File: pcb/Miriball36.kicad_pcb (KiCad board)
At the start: 2 copper layers, 124.8 x 99.1 mm, 45 parts, among them J2 MJ-4PP-9, SW1 SW_PUSH, SW10 SW_PUSH, SW11 SW_PUSH, SW12 SW_PUSH, SW13 SW_PUSH, SW14 SW_PUSH, SW15 SW_PUSH, SW16 SW_PUSH, SW17 SW_PUSH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

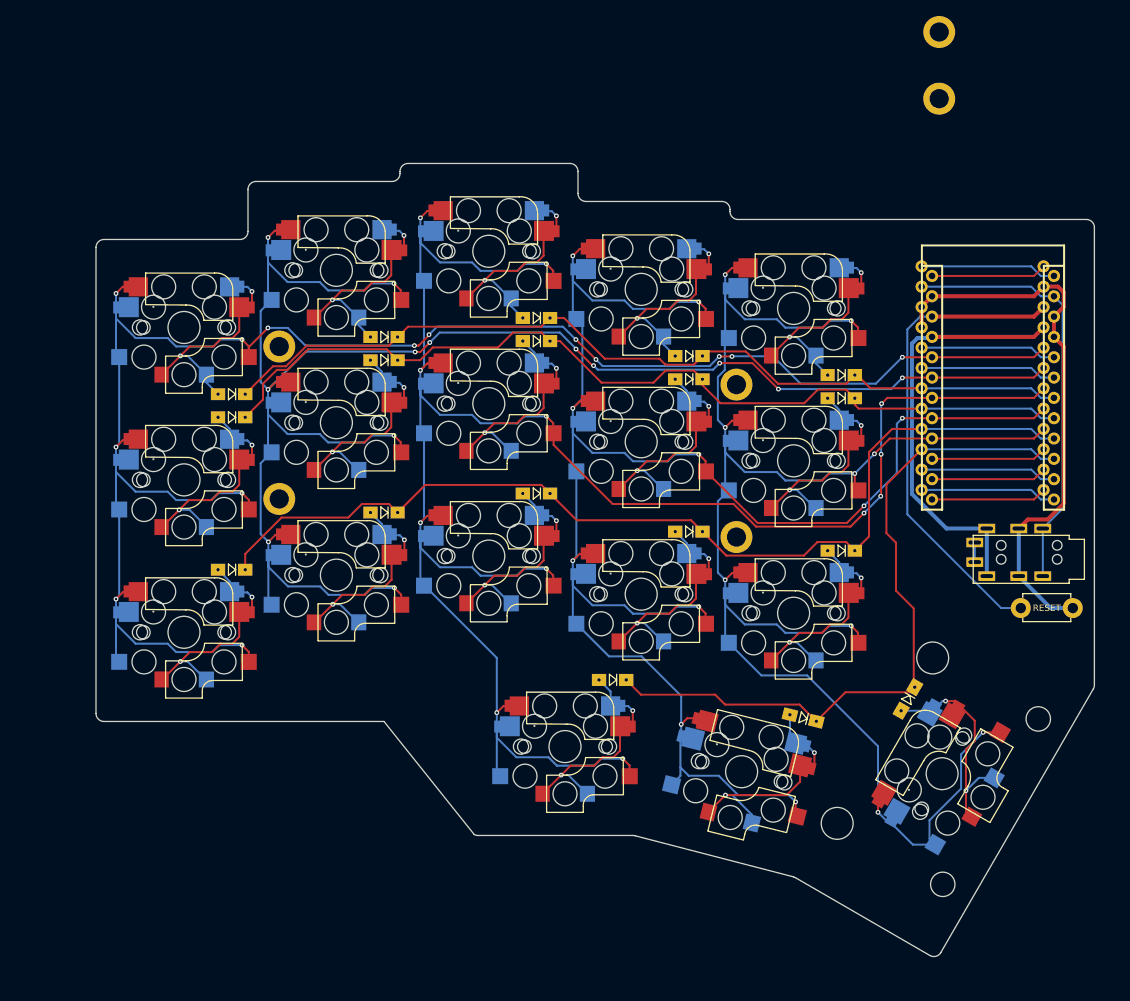
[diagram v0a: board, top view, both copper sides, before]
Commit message: add logo & pin for trackball
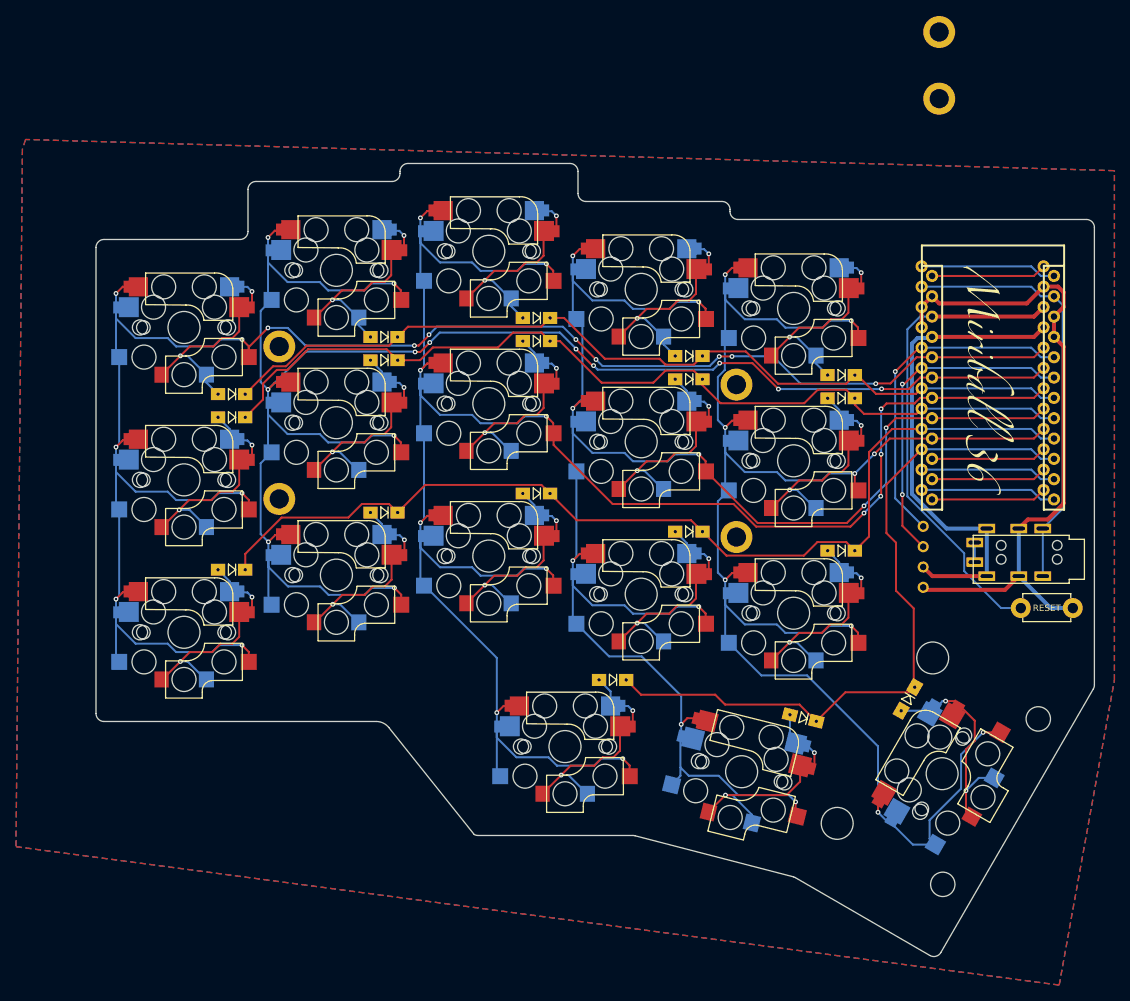
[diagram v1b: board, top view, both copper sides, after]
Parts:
- added G***: LOGO, daiki_daiku_footprints:logo, F.Cu at (157.9, 65.2)
- added OL1: OLED, yuuichi_kbd:OLED_4Pin, F.Cu at (150.2, 87.2)
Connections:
- U1 pad 5: unconnected-(U1-2/D1/SDA-Pad5) -> sda
- U1 pad 6: unconnected-(U1-3/D0/SCL-Pad6) -> scl
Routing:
- net sda: track 0.00 -> 42.4 mm, vias 0 -> 1
- net scl: track 0.00 -> 41.9 mm, vias 0 -> 2
- net unconnected-(U1-3/D0/SCL-Pad6): track 17.0 -> 0.00 mm
- net unconnected-(U1-2/D1/SDA-Pad5): track 17.0 -> 0.00 mm
- net GND: track 70.3 -> 83.9 mm
- net VCC: track 53.2 -> 61.6 mm
- net row0: track 111.4 -> 112.0 mm
- net row1: track 115.8 -> 116.3 mm
- added copper zone on B.Cu, net GND
- added copper zone on F.Cu, net GND
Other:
- outline, holes or cut-outs redrawn

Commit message: add hole
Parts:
- moved H6 71.4 mm to (145.7, 101.0)
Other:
- board text added: "Miriball36 v1.0 PCB Designed by Mimoto & daiki_daiku"
- board text removed: "Miriball39 v1.0 PCB Designed by Mimoto & Mori"
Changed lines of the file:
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@@
 		(fp_arc
 			(start 0.225 -2.8)
-			(mid 1.74436 -2.328061)
+			(mid 1.744359 -2.328061)
 			(end 2.485 -0.920001)
 			(stroke
@@
 		(fp_arc
 			(start 2.57 1.400001)
-			(mid 1.834421 2.975843)
+			(mid 1.834422 2.975844)
 			(end 0.2 3.57)
 			(stroke
@@
 		(fp_arc
 			(start -3.5 6.03)
-			(mid -2.595909 6.48733)
+			(mid -2.59591 6.487331)
 			(end -2.28 7.45)
 			(stroke
@@
 		(fp_arc
 			(start -2.485 -0.920001)
-			(mid -1.74436 -2.328062)
+			(mid -1.74436 -2.328061)
 			(end -0.225 -2.8)
 			(stroke
@@
 		(fp_arc
 			(start 2.57 1.4)
-			(mid 1.834422 2.975842)
+			(mid 1.83442 2.975841)
 			(end 0.2 3.57)
 			(stroke
@@
 		)
 		(pad "1" smd rect
-			(at 8.1 3.700001 166)
+			(at 8.1 3.700002 166)
 			(size 2 2)
 			(layers "F.Cu" "F.Paste" "F.Mask")
@@
 	(footprint "Miriball36:HOLE_M2_CASEPCB"
 		(layer "F.Cu")
-		(at 152.24 29.94)
+		(at 145.74 101.03)
 		(property "Reference" "H6"
 			(at 0 2.7 0)
@@
 		(layer "Edge.Cuts")
 	)
-	(gr_text "Miriball39 v1.0\nPCB Designed by Mimoto & Mori"
+	(gr_text "Miriball36 v1.0\nPCB Designed by Mimoto & daiki_daiku"
 		(at 94.04 107.14 0)
 		(layer "B.Mask")
@@
 		)
 	)
-	(gr_text "Miriball39 v1.0\nPCB Designed by Mimoto & Mori"
-		(at 69.09 107.14 0)
+	(gr_text "Miriball36 v1.0\nPCB Designed by Mimoto & daiki_daiku"
+		(at 63.84 107.14 0)
 		(layer "F.Mask")
 		(effects
@@
 	)
 	(segment
-		(start 66.34 73.24)
-		(end 66.34 75.24)
-		(width 0.25)
-		(layer "F.Cu")
-		(net 31)
-	)
-	(segment
 		(start 55.04 83.64)
 		(end 55.04 83.54)
@@
 	)
 	(segment
+		(start 65.83 73.2)
+		(end 66.34 73.71)
+		(width 0.25)
+		(layer "F.Cu")
+		(net 31)
+	)
+	(segment
+		(start 66.34 73.71)
+		(end 66.34 75.24)
+		(width 0.25)
+		(layer "F.Cu")
+		(net 31)
+	)
+	(segment
 		(start 58.465 80.115)
 		(end 61.265 80.115)
@@
 	)
 	(via
-		(at 66.34 73.24)
+		(at 65.83 73.2)
 		(size 0.6)
 		(drill 0.3)
@@
 	)
 	(segment
-		(start 65.76 72.66)
-		(end 66.34 73.24)
+		(start 65.83 73.2)
+		(end 65.29 72.66)
+		(width 0.25)
+		(layer "B.Cu")
+		(net 31)
+	)
+	(segment
+		(start 65.29 72.66)
+		(end 63.54 72.66)
 		(width 0.25)
 		(layer "B.Cu")
@@
 	)
 	(segment
-		(start 63.54 72.66)
-		(end 65.76 72.66)
-		(width 0.25)
-		(layer "B.Cu")
-		(net 31)
-	)
-	(segment
 		(start 58.54 81.34)
 		(end 60.64 83.44)
@@
 	)
 	(segment
-		(start 66.34 54.04)
-		(end 66.34 56.04)
+		(start 62.56335 59.865)
+		(end 63.888833 59.865)
 		(width 0.25)
 		(layer "F.Cu")
@@
 	)
 	(segment
-		(start 62.56335 59.865)
-		(end 63.888833 59.865)
+		(start 66.34 54.74)
+		(end 66.34 56.04)
 		(width 0.25)
 		(layer "F.Cu")
@@
 	)
 	(segment
+		(start 65.78 54.18)
+		(end 66.34 54.74)
+		(width 0.25)
+		(layer "F.Cu")
+		(net 36)
+	)
+	(segment
 		(start 63.888833 59.865)
 		(end 64.74 59.013833)
@@
 	)
 	(via
-		(at 66.34 54.04)
+		(at 65.78 54.18)
 		(size 0.6)
 		(drill 0.3)
@@
 	)
 	(segment
-		(start 65.76 53.46)
-		(end 66.34 54.04)
+		(start 60.64 64.44)
+		(end 60.64 65.4213)
 		(width 0.25)
 		(layer "B.Cu")
@@
 	)
 	(segment
-		(start 60.64 64.44)
-		(end 60.64 65.4213)
+		(start 65.78 54.18)
+		(end 65.06 53.46)
 		(width 0.25)
 		(layer "B.Cu")
@@
 	)
 	(segment
-		(start 60.64 65.4213)
-		(end 62.09325 66.87455)
+		(start 65.06 53.46)
+		(end 63.54 53.46)
 		(width 0.25)
 		(layer "B.Cu")
@@
 	)
 	(segment
-		(start 57.39 62.09)
-		(end 58.29 62.09)
+		(start 60.64 65.4213)
+		(end 62.09325 66.87455)
 		(width 0.25)
 		(layer "B.Cu")
@@
 	)
 	(segment
-		(start 63.54 53.46)
-		(end 65.76 53.46)
+		(start 57.39 62.09)
+		(end 58.29 62.09)
 		(width 0.25)
 		(layer "B.Cu")

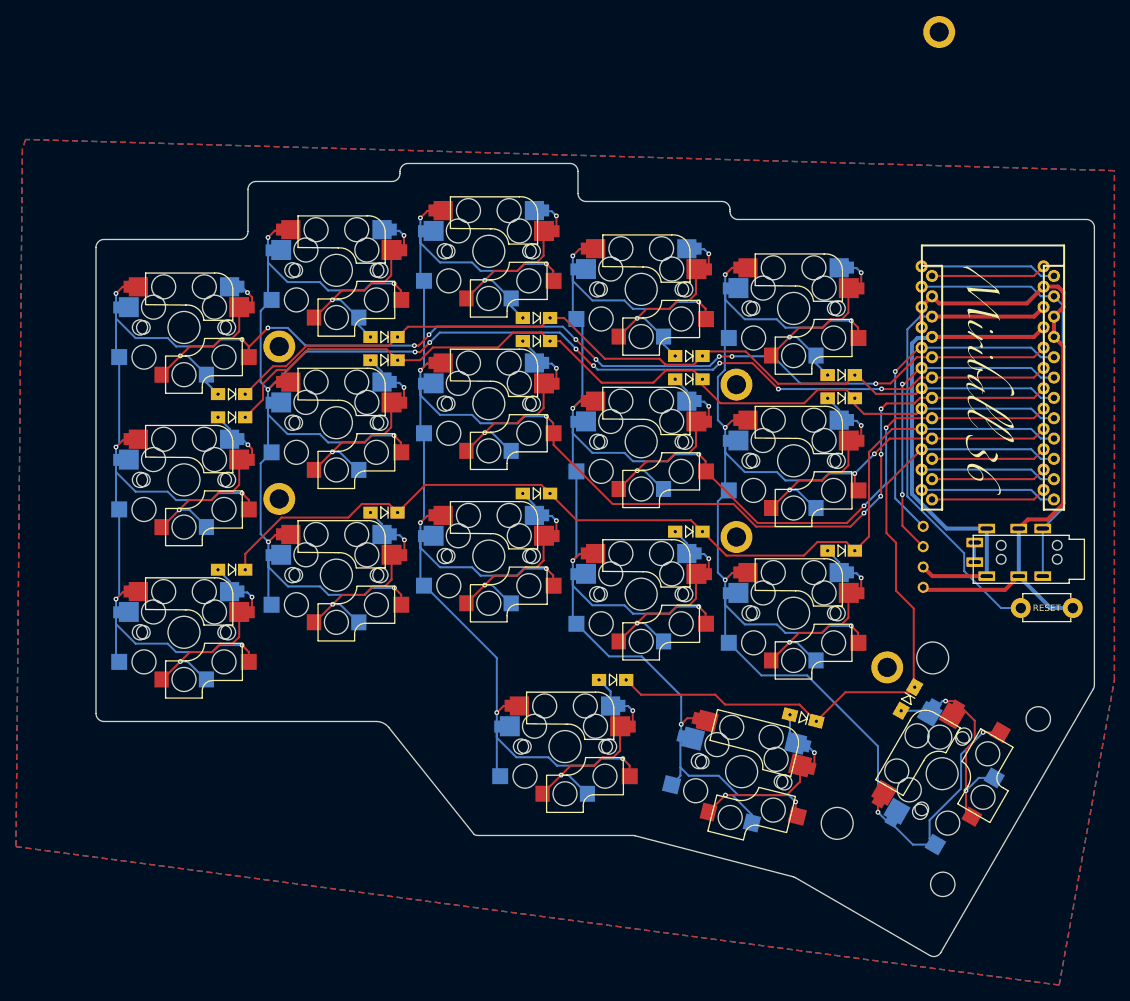
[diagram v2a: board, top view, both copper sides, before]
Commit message: PCBを更新
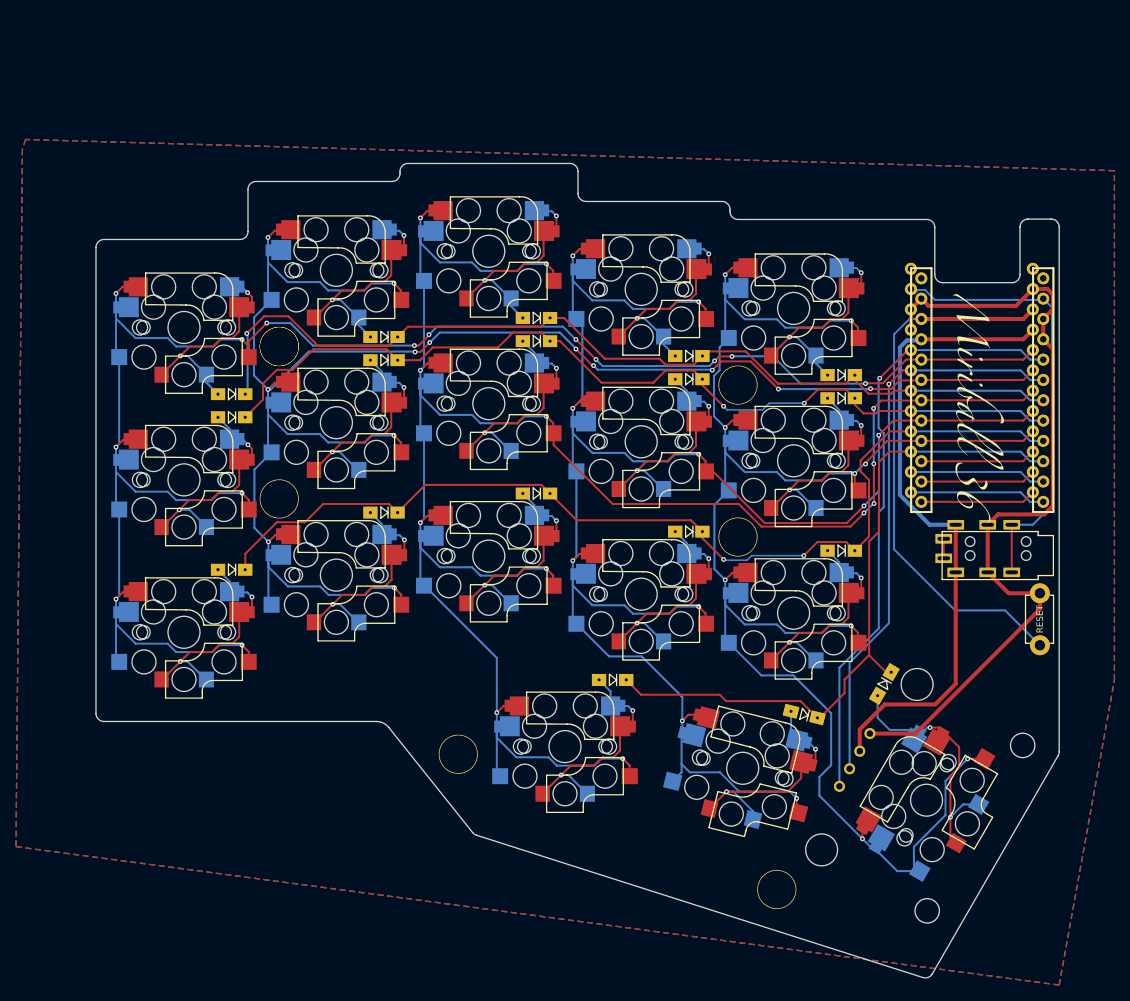
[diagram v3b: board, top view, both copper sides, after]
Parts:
- removed H1, H2, H3, H4, H5, H6: MountingHole, Miriball36:HOLE_M2_CASEPCB
- added ?: , , F.Cu at (69.7, 60.9)
- added ?: , , F.Cu at (69.7, 80.0)
- added ?: , , F.Cu at (127.1, 65.7)
- added ?: , , F.Cu at (127.1, 84.7)
- added TH3: HOLE, yuuichi_kbd:HOLE_M2_TH, F.Cu at (69.7, 60.9)
- added TH3: HOLE, yuuichi_kbd:HOLE_M2_TH, F.Cu at (131.9, 128.8)
- added TH3: HOLE, yuuichi_kbd:HOLE_M2_TH, F.Cu at (92.1, 111.9)
- moved OL1 26.8 mm to (141.7, 112.6), turned to 60 degrees
- moved J2 3.91 mm to (164.6, 87.0)
- moved SW18 3.84 mm to (150.7, 117.6)
- moved G*** 3.68 mm to (156.7, 68.7)
- moved D18 3.49 mm to (145.4, 103.1)
- moved SW19 1.64 mm to (164.8, 95.0), turned to 90 degrees
- moved U1 1.37 mm to (157.5, 66.0)
- moved D17 0.45 mm to (135.4, 106.9)
- moved SW17 0.45 mm to (127.7, 113.6)
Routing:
- net sda: track 42.4 -> 76.0 mm
- net scl: track 41.9 -> 70.6 mm, vias 2 -> 1
- net VCC: track 61.6 -> 81.5 mm
- net GND: track 83.9 -> 102.2 mm
- net unconnected-(U1-TX0/D3-Pad1): track 17.0 -> 0.00 mm
- net unconnected-(U1-RAW-Pad24): track 14.4 -> 0.00 mm
- net reset: track 60.3 -> 68.7 mm
- net row0: track 112.0 -> 118.4 mm, vias 0 -> 1
- net Net-(D18-A): track 28.0 -> 32.9 mm
- net row3: track 90.0 -> 86.7 mm
- net data: track 53.5 -> 55.7 mm
- net col4: track 205.7 -> 207.8 mm
- net col3: track 220.5 -> 218.7 mm
- net col2: track 247.9 -> 247.1 mm
- net row1: track 116.3 -> 115.5 mm, vias 0 -> 2
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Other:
- board size 124.8 x 99.1 mm -> 120.4 x 101.8 mm

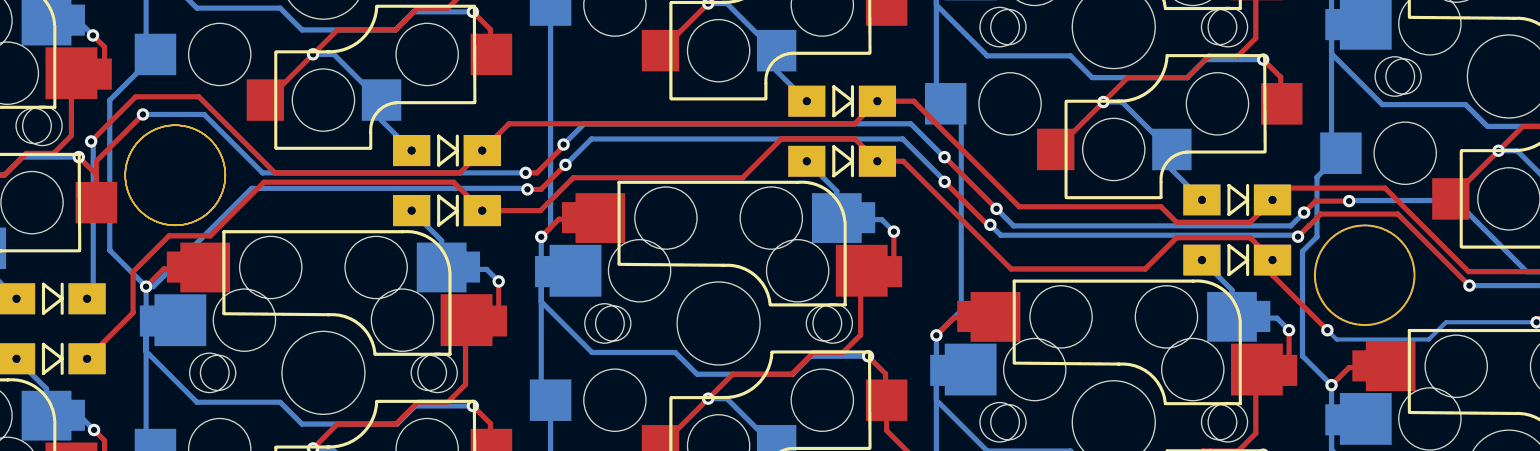
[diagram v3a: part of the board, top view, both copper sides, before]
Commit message: change hole
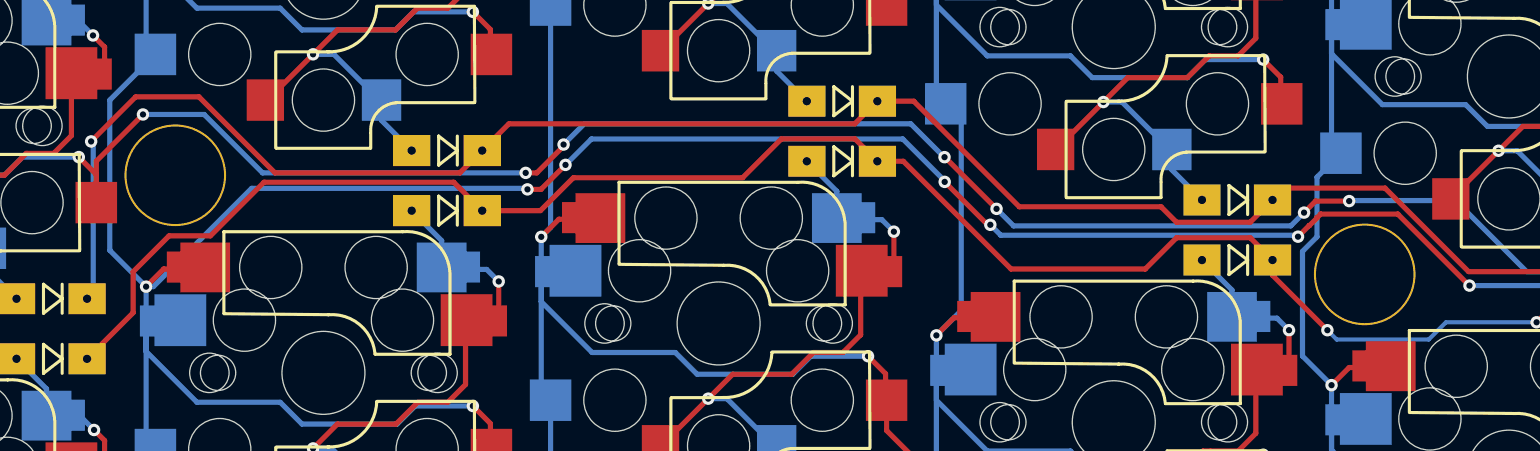
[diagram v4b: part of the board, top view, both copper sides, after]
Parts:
- removed the ? at (69.7, 60.9)
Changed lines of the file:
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@@
 				(type solid)
 			)
-			(layer "B.SilkS")
+			(layer "Eco1.User")
 		)
 		(fp_line
@@
 				(type solid)
 			)
-			(layer "B.SilkS")
+			(layer "Eco1.User")
 		)
 		(fp_line
@@
 				(type solid)
 			)
-			(layer "B.SilkS")
+			(layer "Eco1.User")
 		)
 		(fp_line
@@
 				(type solid)
 			)
-			(layer "B.SilkS")
+			(layer "Eco1.User")
 		)
 		(pad "1" thru_hole circle
@@
 		)
 	)
-	(footprint ""
-		(layer "F.Cu")
-		(at 69.7465 60.9213)
-		(property "Reference" ""
-			(at 0 0 0)
-			(unlocked yes)
-			(layer "F.SilkS")
-			(effects
-				(font
-					(size 1.27 1.27)
-				)
-			)
-		)
-		(property "Value" ""
-			(at 0 0 0)
-			(unlocked yes)
-			(layer "F.Fab")
-			(effects
-				(font
-					(size 1.27 1.27)
-				)
-			)
-		)
-		(property "Footprint" ""
-			(at 0 0 0)
-			(unlocked yes)
-			(layer "F.Fab")
-			(hide yes)
-			(effects
-				(font
-					(size 1.27 1.27)
-				)
-			)
-		)
-		(property "Datasheet" ""
-			(at 0 0 0)
-			(unlocked yes)
-			(layer "F.Fab")
-			(hide yes)
-			(effects
-				(font
-					(size 1.27 1.27)
-				)
-			)
-		)
-		(property "Description" ""
-			(at 0 0 0)
-			(unlocked yes)
-			(layer "F.Fab")
-			(hide yes)
-			(effects
-				(font
-					(size 1.27 1.27)
-				)
-			)
-		)
-		(pad "" thru_hole circle
-			(at 0 0 90)
-			(size 4.9 4.9)
-			(drill 4.7)
-			(layers "*.Cu" "*.Mask")
-			(remove_unused_layers no)
-			(clearance 0.3)
-		)
-	)
 	(footprint "Miriball36:Diode_1N4148W"
 		(placed yes)
@@
 	(footprint ""
 		(layer "F.Cu")
-		(at 127.09 65.74)
+		(at 127.09 65.7)
 		(property "Reference" ""
 			(at 0 0 0)

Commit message: add Gerber
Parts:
- moved G*** 1.25 mm to (156.7, 67.4)
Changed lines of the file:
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@@
 	(footprint "daiki_daiku_footprints:logo"
 		(layer "F.Cu")
-		(at 156.651124 68.69 -90)
+		(at 156.74 67.44 -90)
 		(property "Reference" "G***"
 			(at 0 0 90)
